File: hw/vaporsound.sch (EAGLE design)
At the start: 57 parts

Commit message: schematics done-ish
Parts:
- removed IC1: (no value), SparkFun-PowerIC:V_REG_LM1117SOT223
- added Q1, Q2: BSS138, SparkFun-DiscreteSemi:MOSFET-NCHANNELBSS138
- added R11, R12, R13, R14: 4k7, rcl:R-EU_R0603
- added SV1: (no value), con-lstb:MA04-1
- added SV2: (no value), con-lstb:MA03-1
- added U$4: MA23-2, con-lstb-mod:MA23-2
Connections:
- new net N$24: C7.-, SV2.3
- new net N$29: C8.-, SV2.1
- new net SCL5V: Q2.D, R13.1, SV1.4
- new net SDA5V: Q1.D, R14.1, SV1.3
- net +3V3: now also Q1.G, Q2.G, R11.2, R12.2, U$4.3, U$4.4; no longer IC1.OUT, IC1.OUT@1
- net +5V: now also R13.2, R14.2, SV1.2, U$4.5, U$4.6; no longer IC1.IN
- net BCK: now also U$4.31
- net D_ADC: now also U$4.30
- net D_AMP: now also U$4.28
- net GND: now also SV1.1, SV2.2, U$4.1, U$4.2, U$4.43, U$4.44, U$4.45, U$4.46; no longer IC1.ADJ
- net LRCK: now also U$4.29
- net MCK: now also U$4.25
- net POWERDOWN: now also U$4.23
- net RESET: now also U$4.15
- net SCL: now also Q2.S, R12.1, U$4.19
- net SDA: now also Q1.S, R11.1, U$4.20

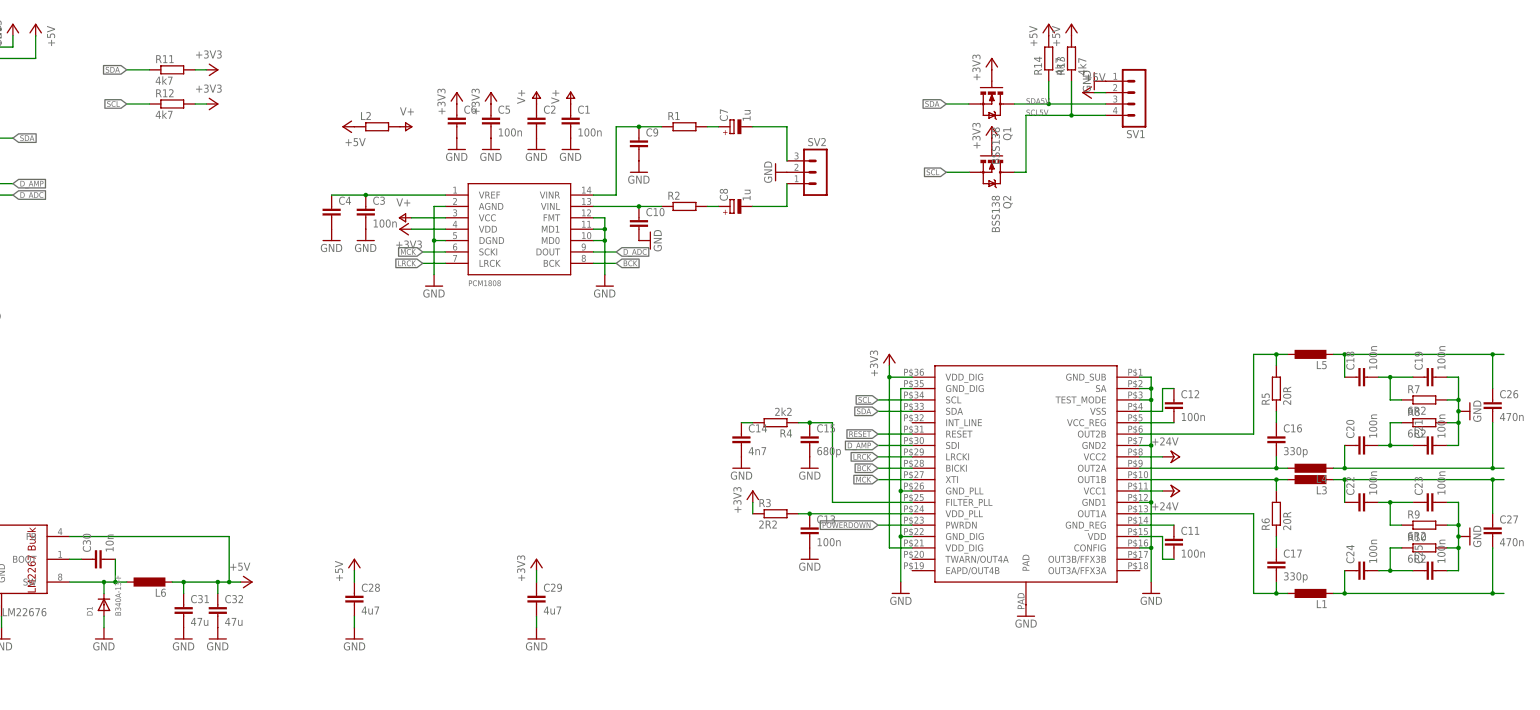
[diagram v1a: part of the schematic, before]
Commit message: layout voltage regulator and add some capacitors
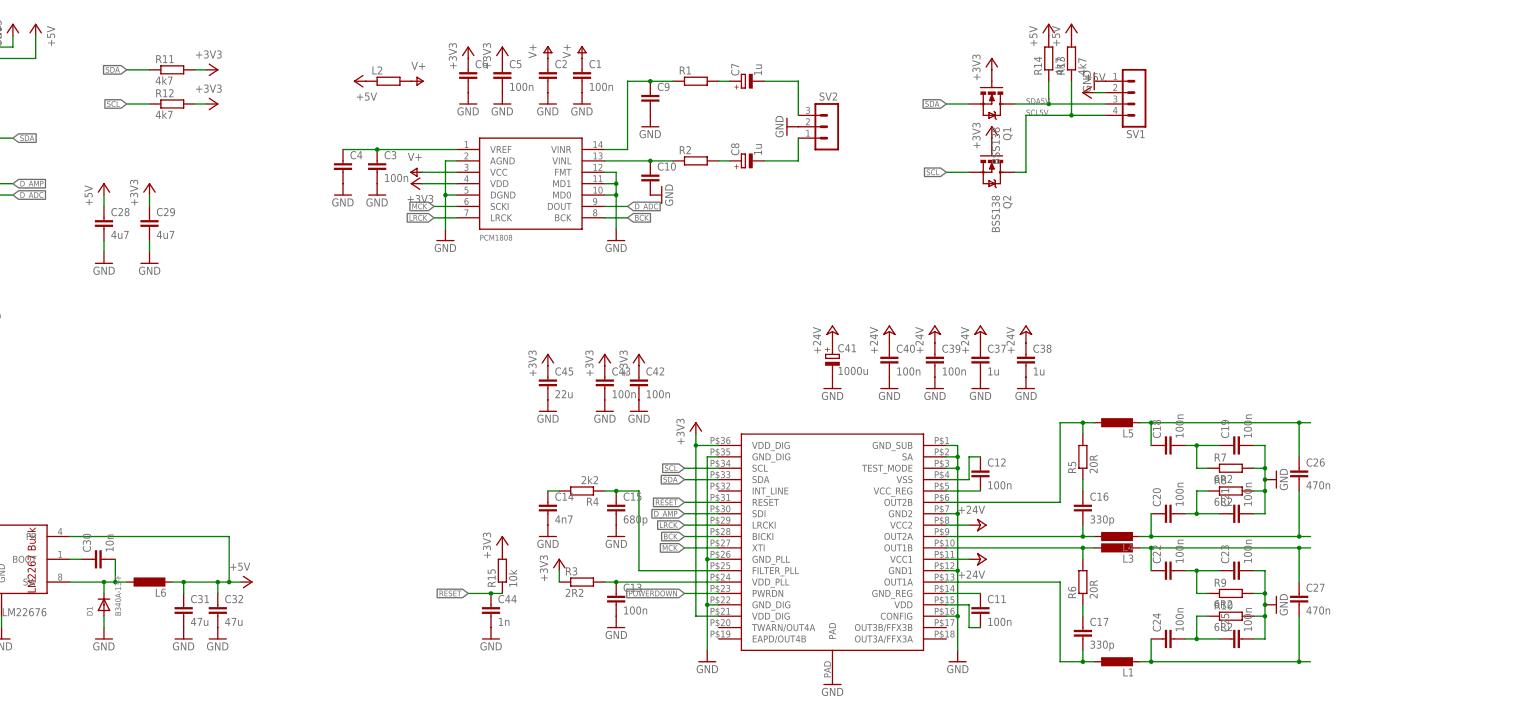
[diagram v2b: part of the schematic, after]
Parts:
- added C37, C38: 1u, rcl:C-EUC0805
- added C39, C40: 100n, rcl:C-EUC0603
- added C41: 1000u, rcl:CPOL-EUE5-10.5
- added C42, C43: 100n, rcl:C-EUC0402
- added C44: 1n, rcl:C-EUC0603
- added C45: 22u, rcl:C-EUC1206
- added R15: 10k, rcl:R-EU_R0603
- C11, C12: device rcl:C-EUC0402 -> rcl:C-EUC0603
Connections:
- net N$23 renamed SW
- net +24V: now also C37.1, C38.1, C39.1, C40.1, C41.+
- net +3V3: now also C42.1, C43.1, C45.1, R15.2
- net GND: now also C37.2, C38.2, C39.2, C40.2, C41.-, C42.2, C43.2, C44.2, C45.2
- net RESET: now also C44.1, R15.1
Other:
- moved on the sheet: C1, C10, C11, C12, C13, C14, C15, C16, C17, C18, C19, C2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

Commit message: begin layout of 24v side of sta350
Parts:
- C37, C38: device rcl:C-EUC0805 -> rcl:C-EUC1206
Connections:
- net N$14 renamed OUT2A
- net N$15 renamed OUT2B
- net N$16 renamed OUT1B
- net N$17 renamed OUT1A
- net N$18 renamed SPKR2B
- net N$20 renamed SPKR2A
- net N$25 renamed SPKR1B
- net N$26 renamed SPKR1A
- net N$6 renamed GND_REG
- net N$7 renamed VDD
- net N$8 renamed VSS
- net N$9 renamed VCC_REG
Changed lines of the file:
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@@
 <part name="SV2" library="con-lstb" deviceset="MA03-1" device=""/>
 <part name="GND34" library="supply1" deviceset="GND" device=""/>
-<part name="C37" library="rcl" deviceset="C-EU" device="C0805" value="1u"/>
-<part name="C38" library="rcl" deviceset="C-EU" device="C0805" value="1u"/>
+<part name="C37" library="rcl" deviceset="C-EU" device="C1206" value="1u"/>
+<part name="C38" library="rcl" deviceset="C-EU" device="C1206" value="1u"/>
 <part name="C39" library="rcl" deviceset="C-EU" device="C0603" value="100n"/>
 <part name="C40" library="rcl" deviceset="C-EU" device="C0603" value="100n"/>
@@
 </segment>
 </net>
-<net name="N$6" class="0">
+<net name="GND_REG" class="0">
 <segment>
 <pinref part="U$1" gate="G$1" pin="GND_REG"/>
@@
 </segment>
 </net>
-<net name="N$7" class="0">
+<net name="VDD" class="0">
 <segment>
 <pinref part="U$1" gate="G$1" pin="VDD"/>
@@
 </segment>
 </net>
-<net name="N$8" class="0">
+<net name="VSS" class="0">
 <segment>
 <pinref part="U$1" gate="G$1" pin="VSS"/>
@@
 </segment>
 </net>
-<net name="N$9" class="0">
+<net name="VCC_REG" class="0">
 <segment>
 <pinref part="C12" gate="G$1" pin="2"/>
@@
 </segment>
 </net>
-<net name="N$15" class="0">
+<net name="OUT2B" class="0">
 <segment>
 <pinref part="U$1" gate="G$1" pin="OUT2B"/>
@@
 </segment>
 </net>
-<net name="N$17" class="0">
+<net name="OUT1A" class="0">
 <segment>
 <pinref part="U$1" gate="G$1" pin="OUT1A"/>
@@
 </segment>
 </net>
-<net name="N$18" class="0">
+<net name="SPKR2B" class="0">
 <segment>
 <pinref part="C18" gate="G$1" pin="1"/>
@@
 </segment>
 </net>
-<net name="N$20" class="0">
+<net name="SPKR2A" class="0">
 <segment>
 <pinref part="L4" gate="G$1" pin="2"/>
@@
 </segment>
 </net>
-<net name="N$14" class="0">
+<net name="OUT2A" class="0">
 <segment>
 <pinref part="U$1" gate="G$1" pin="OUT2A"/>
@@
 </segment>
 </net>
-<net name="N$16" class="0">
+<net name="OUT1B" class="0">
 <segment>
 <pinref part="U$1" gate="G$1" pin="OUT1B"/>
@@
 </segment>
 </net>
-<net name="N$25" class="0">
+<net name="SPKR1B" class="0">
 <segment>
 <pinref part="L3" gate="G$1" pin="2"/>
@@
 </segment>
 </net>
-<net name="N$26" class="0">
+<net name="SPKR1A" class="0">
 <segment>
 <pinref part="L1" gate="G$1" pin="2"/>

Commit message: output stage almost routed
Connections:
- removed net N$13: C17.1, R6.1
- new net N$6: C17.2, R6.2
- net OUT1A: now also R6.1; no longer C17.2
- net OUT1B: now also C17.1; no longer R6.2
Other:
- moved on the sheet: C17, R6
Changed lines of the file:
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@@
 <instance part="L5" gate="G$1" x="279.4" y="71.12" rot="R90"/>
 <instance part="C16" gate="G$1" x="271.78" y="53.34"/>
-<instance part="C17" gate="G$1" x="271.78" y="25.4"/>
+<instance part="C17" gate="G$1" x="271.78" y="38.1"/>
 <instance part="R5" gate="G$1" x="271.78" y="63.5" rot="R90"/>
-<instance part="R6" gate="G$1" x="271.78" y="35.56" rot="R90"/>
+<instance part="R6" gate="G$1" x="271.78" y="25.4" rot="R90"/>
 <instance part="C18" gate="G$1" x="289.56" y="66.04" rot="R90"/>
 <instance part="C19" gate="G$1" x="304.8" y="66.04" rot="R90"/>
@@
 </segment>
 </net>
-<net name="N$13" class="0">
-<segment>
-<pinref part="R6" gate="G$1" pin="1"/>
-<pinref part="C17" gate="G$1" pin="1"/>
-<wire x1="271.78" y1="30.48" x2="271.78" y2="27.94" width="0.1524" layer="91"/>
-</segment>
-</net>
 <net name="OUT2B" class="0">
 <segment>
@@
 <wire x1="241.3" y1="35.56" x2="266.7" y2="35.56" width="0.1524" layer="91"/>
 <wire x1="266.7" y1="35.56" x2="266.7" y2="17.78" width="0.1524" layer="91"/>
-<pinref part="C17" gate="G$1" pin="2"/>
+<wire x1="274.32" y1="17.78" x2="271.78" y2="17.78" width="0.1524" layer="91"/>
+<pinref part="L1" gate="G$1" pin="1"/>
+<pinref part="R6" gate="G$1" pin="1"/>
+<wire x1="271.78" y1="17.78" x2="266.7" y2="17.78" width="0.1524" layer="91"/>
 <wire x1="271.78" y1="20.32" x2="271.78" y2="17.78" width="0.1524" layer="91"/>
-<wire x1="271.78" y1="17.78" x2="266.7" y2="17.78" width="0.1524" layer="91"/>
-<pinref part="L1" gate="G$1" pin="1"/>
-<wire x1="271.78" y1="17.78" x2="274.32" y2="17.78" width="0.1524" layer="91"/>
 <junction x="271.78" y="17.78"/>
 </segment>
@@
 <pinref part="L3" gate="G$1" pin="1"/>
 <wire x1="241.3" y1="43.18" x2="271.78" y2="43.18" width="0.1524" layer="91"/>
-<pinref part="R6" gate="G$1" pin="2"/>
+<pinref part="C17" gate="G$1" pin="1"/>
 <wire x1="271.78" y1="43.18" x2="274.32" y2="43.18" width="0.1524" layer="91"/>
-<wire x1="271.78" y1="40.64" x2="271.78" y2="43.18" width="0.1524" layer="91"/>
+<wire x1="271.78" y1="43.18" x2="271.78" y2="40.64" width="0.1524" layer="91"/>
 <junction x="271.78" y="43.18"/>
 </segment>
@@
 </segment>
 </net>
+<net name="N$6" class="0">
+<segment>
+<pinref part="C17" gate="G$1" pin="2"/>
+<pinref part="R6" gate="G$1" pin="2"/>
+<wire x1="271.78" y1="33.02" x2="271.78" y2="30.48" width="0.1524" layer="91"/>
+</segment>
+</net>
